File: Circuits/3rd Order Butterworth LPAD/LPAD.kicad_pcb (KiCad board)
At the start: 2 copper layers, 116.8 x 162.6 mm, 30 parts, among them P1 INPUT, P2 TWEETER, P3 WOOFER_A, P4 WOOFER_B, SW1 Attenuation, SW2 Phase, SW3 Attenuation, SW4 Phase, SW5 Bypass, SW6 Phase

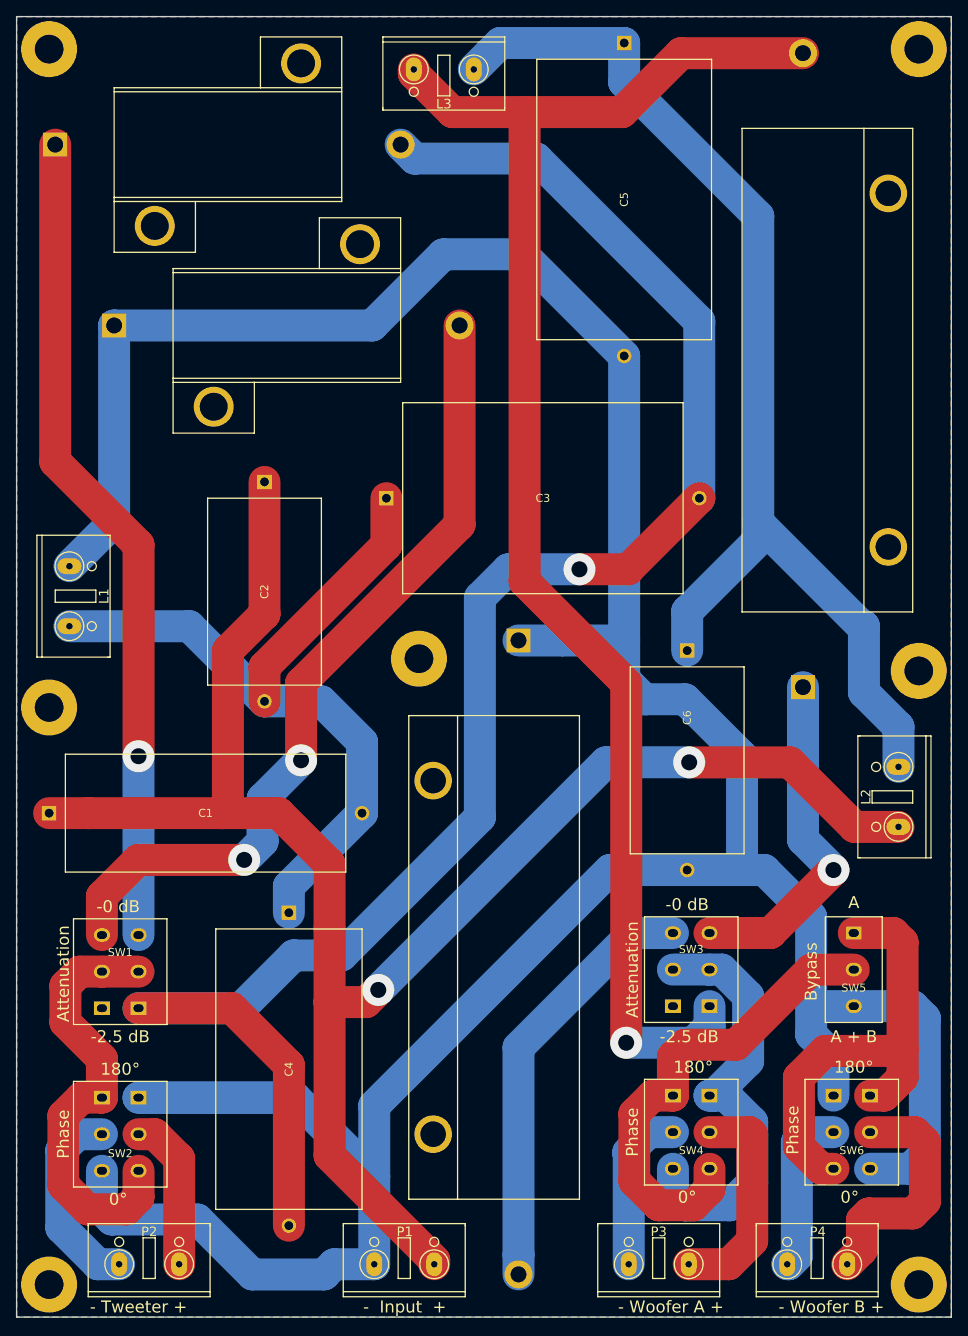
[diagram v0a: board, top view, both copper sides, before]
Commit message: Circuits: Updated 3d models on LPAD
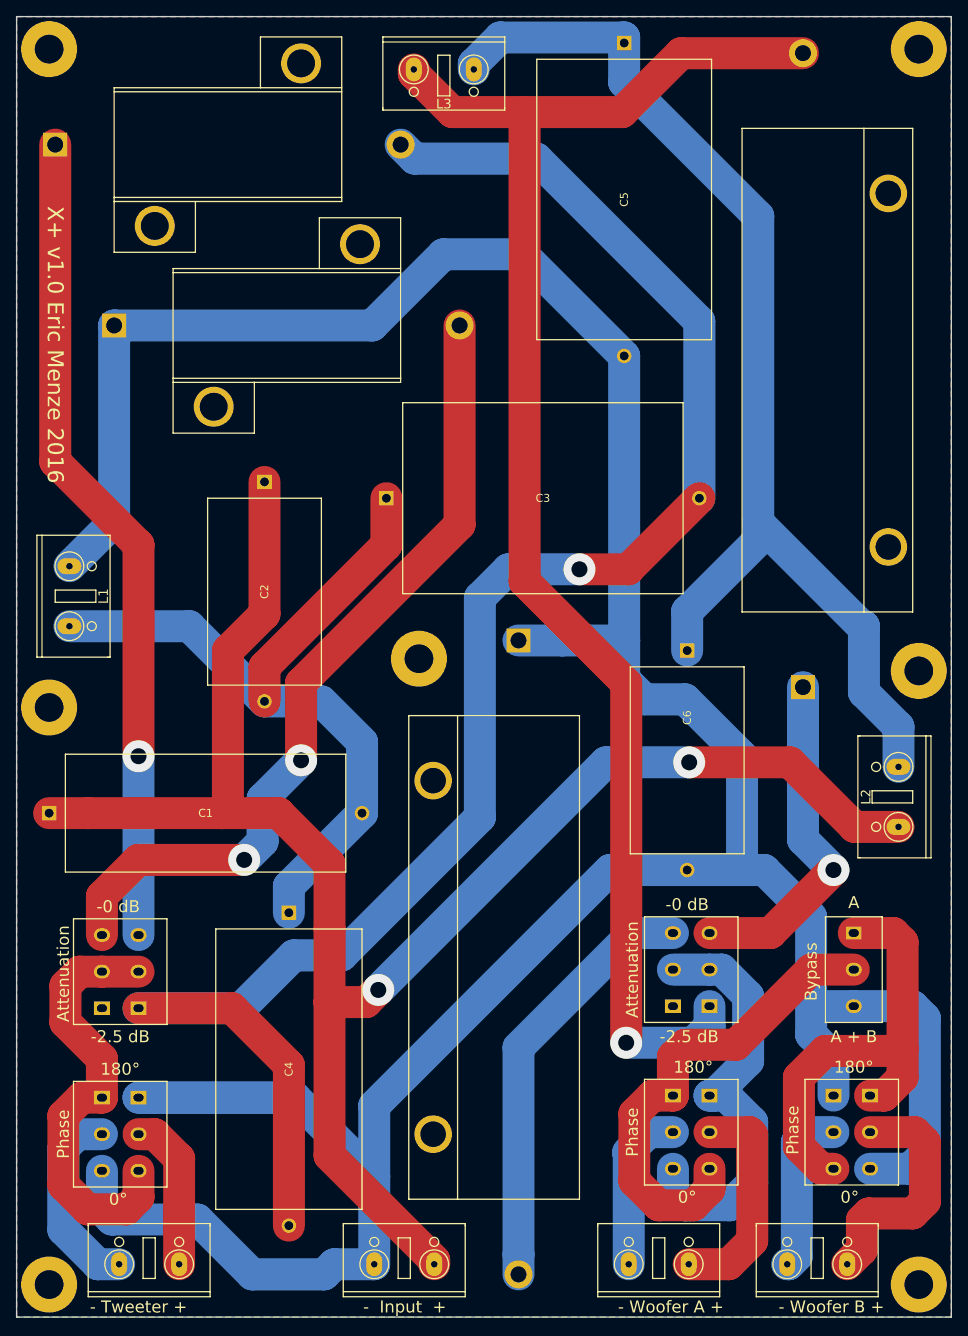
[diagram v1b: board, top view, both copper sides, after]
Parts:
- P1: value INPUT -> Input
- P2: value TWEETER -> Tweeter
- P3: value WOOFER_A -> Woofer A
- P4: value WOOFER_B -> Woofer B
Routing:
- net Net-(C5-Pad1): track 144.7 -> 146.1 mm
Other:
- board text added: "X+ v1.0 Eric Menze 2016"

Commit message: Circuits: Updating X+ - reducing via count, updating resistor footprints
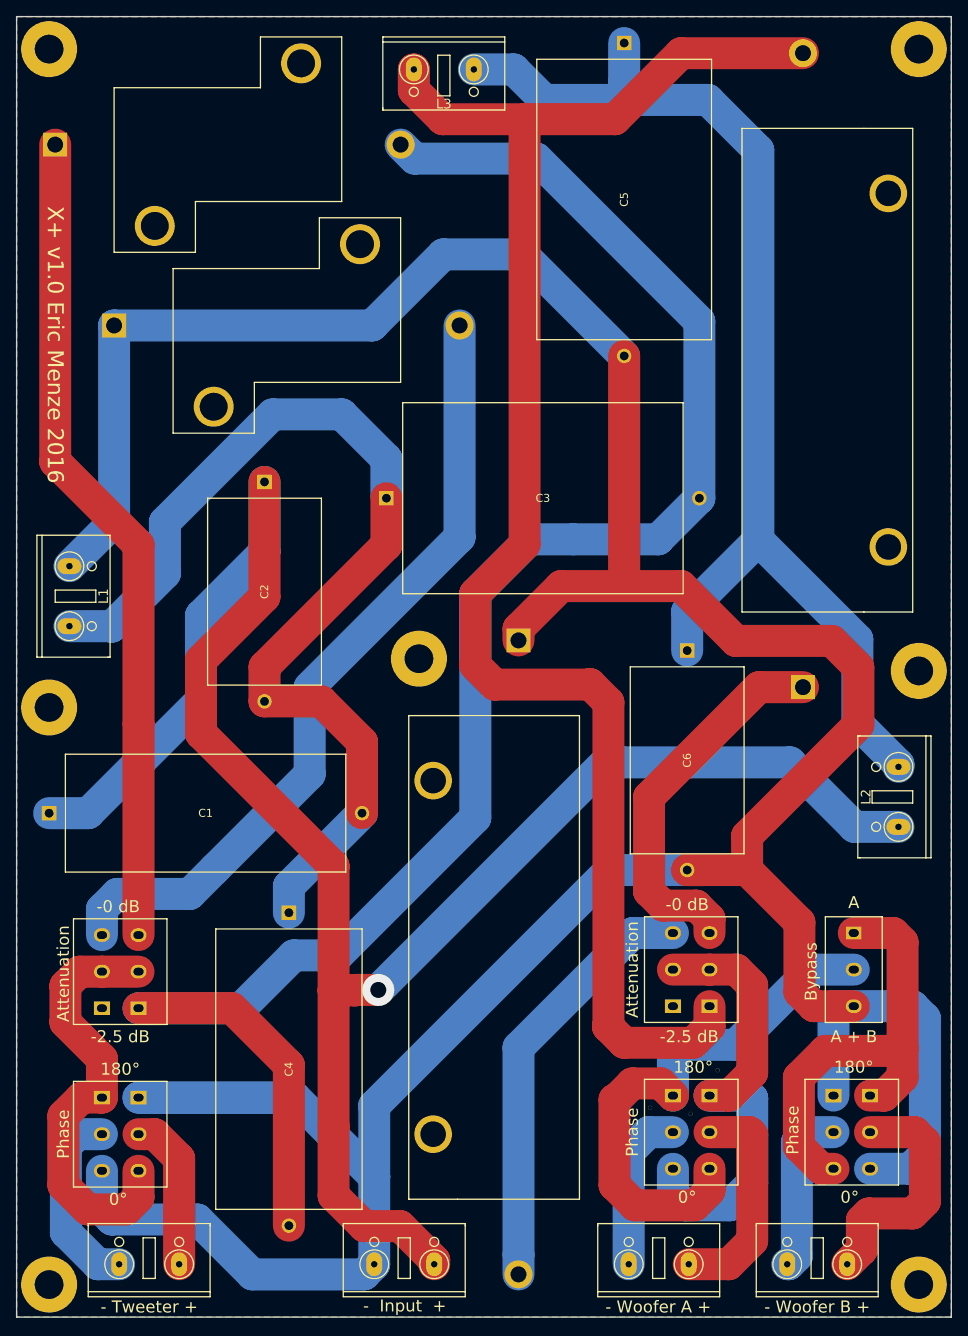
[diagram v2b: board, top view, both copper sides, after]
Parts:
- added ?: , Footprints:Thermal_Via_NoRing, F.Cu at (125.7, 152.0)
- added ?: , Footprints:Thermal_Via_NoRing, F.Cu at (122.4, 157.5)
- added ?: , Footprints:Thermal_Via_NoRing, F.Cu at (117.3, 156.7)
- P1: value Input -> INPUT
- P2: value Tweeter -> TWEETER
- P3: value Woofer A -> WOOFER_A
- P4: value Woofer B -> WOOFER_B
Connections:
- net Net-(C1-Pad2) renamed /High_Xover
- net Net-(C3-Pad2) renamed /High
- net Net-(C5-Pad1) renamed /Low_Xover
- net Net-(L3-Pad1) renamed /Low
- net Net-(R2-Pad2) renamed /High_Shunt
- net Net-(R4-Pad2) renamed /Low_Shunt
- net Net-(SW1-Pad2) renamed /High_Attenuated
- net Net-(SW3-Pad2) renamed /Low_Attenuated
- net Net-(SW4-Pad1) renamed /Bypass
- net Net-(SW5-Pad1) renamed /Low_Secondary
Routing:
- net /IN+: track 223.6 -> 257.0 mm, vias 2 -> 1
- net /High_Xover: track 99.4 -> 132.7 mm
- net /IN-: track 438.6 -> 464.2 mm
- net /Low: track 189.6 -> 203.1 mm, vias 1 -> 0
- net /Bypass: track 60.2 -> 67.8 mm
- net /Low_Attenuated: track 54.6 -> 59.0 mm
- net Net-(R3-Pad1): track 43.2 -> 47.5 mm, vias 1 -> 0
- net /Low_Xover: track 146.1 -> 148.7 mm
- net /High_Shunt: track 102.5 -> 100.0 mm, vias 2 -> 0
- net /High: track 223.0 -> 223.3 mm, vias 1 -> 0
- net Net-(R1-Pad1): vias 1 -> 0
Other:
- board text added: "X+"
